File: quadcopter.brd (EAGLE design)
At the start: 137.4 x 137.4 mm, 73 parts, among them J1 AVR_SPI_PRG_6NS, U3 ATMEGA128RFA1

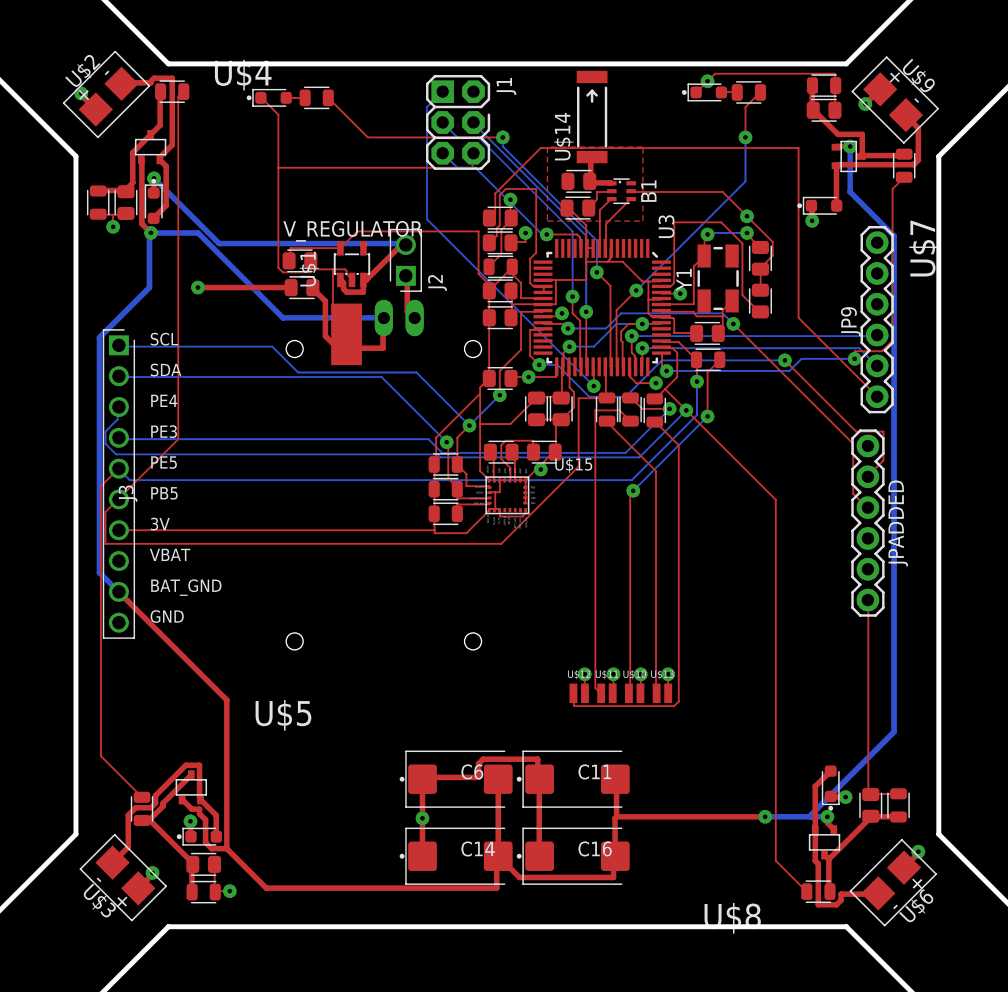
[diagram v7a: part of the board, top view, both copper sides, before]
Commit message: added faraday cage to antenna
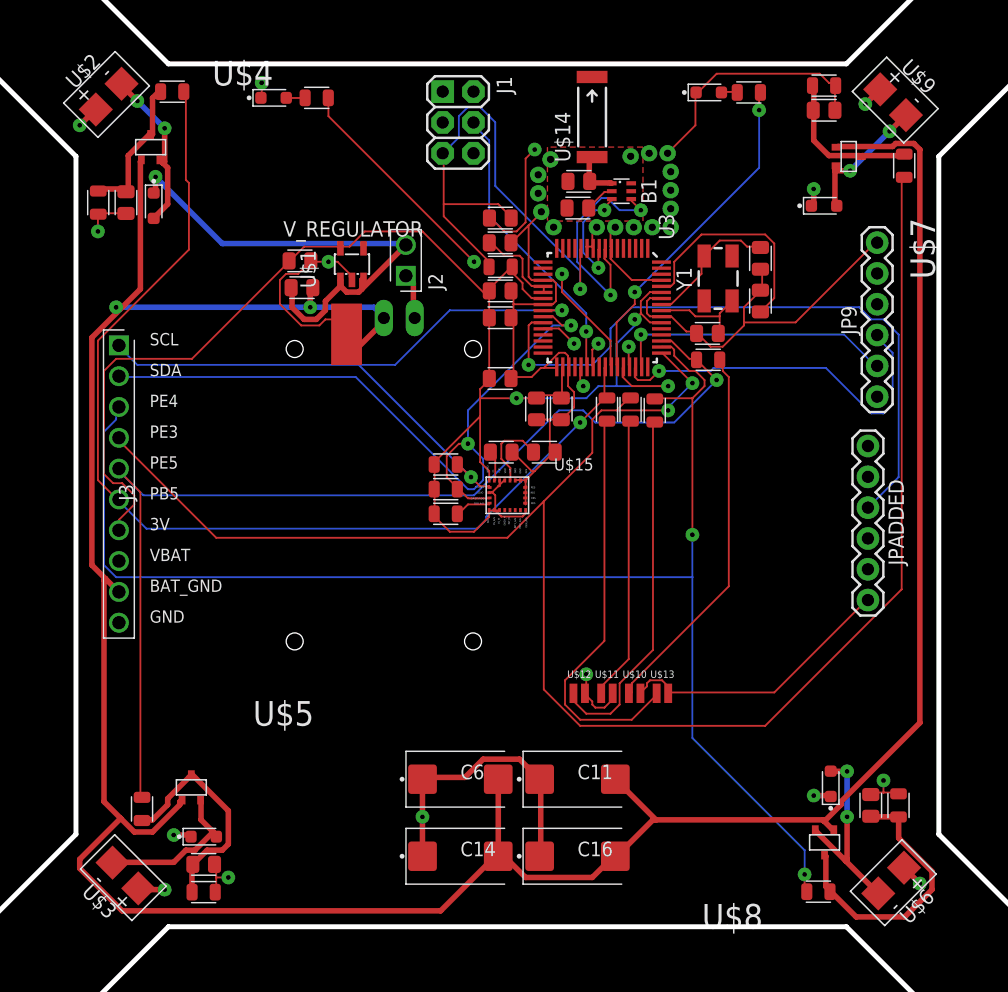
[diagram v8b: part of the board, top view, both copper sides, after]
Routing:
- net PE3: track 89.8 -> 148.0 mm, vias 3 -> 2
- net RESET: track 21.7 -> 44.5 mm, vias 2 -> 1
- net RX1: track 36.8 -> 54.1 mm, vias 2 -> 1
- net RFP: track 4.98 -> 18.9 mm, vias 0 -> 2
- net FILTEREDNE: track 10.5 -> 22.8 mm
- net PE4: track 105.8 -> 117.2 mm, vias 1 -> 2
- net 3V: track 130.3 -> 141.1 mm
- net BAT_GND: track 234.8 -> 245.5 mm, vias 4 -> 2
- net TX1: track 41.7 -> 31.9 mm, vias 2 -> 1
- net DVDD: track 17.2 -> 7.40 mm
- net N$11: track 24.1 -> 33.9 mm
- net SDA: track 53.3 -> 62.7 mm
- net RX0: track 22.9 -> 30.7 mm
- net PB5: track 92.2 -> 86.3 mm, vias 0 -> 1
- net FILTEREDSW: track 13.2 -> 18.9 mm
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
